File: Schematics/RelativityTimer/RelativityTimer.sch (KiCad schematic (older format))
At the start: 11 parts, among them J1 Conn_01x12_Female, SW1 SW_Push, SW2 SW_Push, SW3 SW_Push

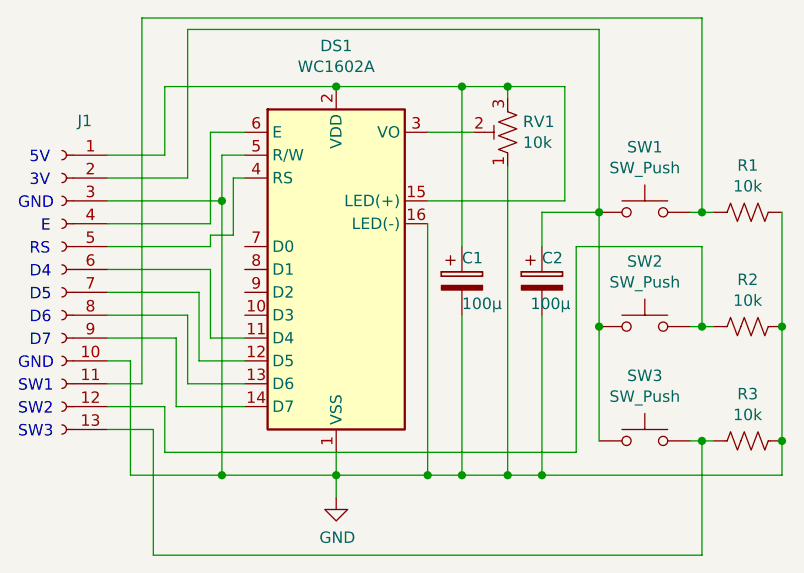
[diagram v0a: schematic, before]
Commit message: Add protection diode for LCD
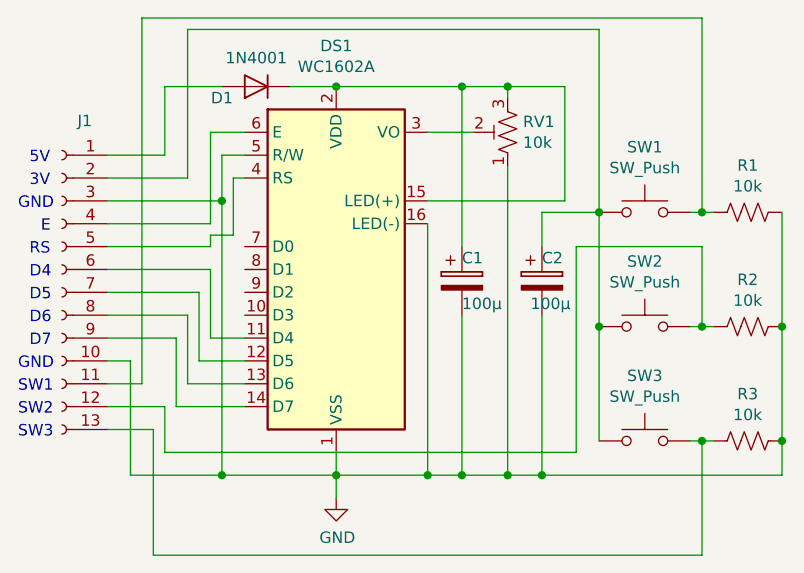
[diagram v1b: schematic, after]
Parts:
- added D1: 1N4001, Diode_THT:D_DO-41_SOD81_P10.16mm_Horizontal, symbol Diode:1N4001
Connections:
- net at C1.1, DS1.15 (LED(+)), DS1.2 (VDD)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: now also D1.1 (K); no longer J1.1 (Pin_1)
- new net: D1.2 (A), J1.1 (Pin_1)
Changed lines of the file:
@@
 	4700 3150 4700 2850
-Wire Wire Line
-	4700 2850 5450 2850
-Connection ~ 5450 2850
 Wire Wire Line
 	4800 3250 4800 2600
@@
 Wire Wire Line
 	6350 3400 6600 3400
+$Comp
+L Diode:1N4001 D1
+U 1 1 5C6E90ED
+P 5100 2850
+F 0 "D1" H 5250 2900 50  0000 C CNN
+F 1 "1N4001" H 5100 2725 50  0000 C CNN
+F 2 "Diode_THT:D_DO-41_SOD81_P10.16mm_Horizontal" H 5100 2675 50  0001 C CNN
+F 3 "http://www.vishay.com/docs/88503/1n4001.pdf" H 5100 2850 50  0001 C CNN
+	1    5100 2850
+	-1   0    0    1
+$EndComp
+Wire Wire Line
+	4950 2850 4700 2850
+Wire Wire Line
+	5250 2850 5450 2850
+Connection ~ 5450 2850
 $EndSCHEMATC
